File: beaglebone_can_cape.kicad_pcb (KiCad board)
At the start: 2 copper layers, 86.4 x 54.6 mm, 24 parts, among them J1 DCAN0, J2 DCAN1, P8 BeagleBone_Black_Header, P9 BeagleBone_Black_Header, U1 TCAN332, U2 TCAN332, U3 LMR51430

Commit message: PCB and SCH updates
Just moved some text boxes, footprints, and explored ideas for the Deutsch connectors.

Co-Authored-By: Zach Weidner <119375087+weidnerz@users.noreply.github.com>
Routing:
- added copper zone on F.Cu, net +3.3V
- added copper zone on B.Cu, net GNDD
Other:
- board text added: "DCAN0"
- board text added: "DCAN1"
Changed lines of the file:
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@@
 	(net 99 "unconnected-(U2-NC-Pad5)")
 	(footprint "Connector_PinHeader_2.54mm:PinHeader_2x23_P2.54mm_Vertical"
-		(locked yes)
 		(layer "F.Cu")
 		(at 119.685 49.835 90)
@@
 		(tags "Through hole pin header THT 2x23 2.54mm double row")
 		(property "Reference" "P8"
-			(at 1.27 -2.33 270)
+			(at -2.165 0 0)
 			(layer "F.SilkS")
 			(effects
@@
 			)
 			(rotate
-				(xyz 0 0 0)
+				(xyz -0 -0 -0)
 			)
 		)
 	)
 	(footprint "Connector_PinHeader_2.54mm:PinHeader_2x23_P2.54mm_Vertical"
-		(locked yes)
 		(layer "F.Cu")
 		(at 119.685 98.095 90)
@@
 		(tags "Through hole pin header THT 2x23 2.54mm double row")
 		(property "Reference" "P9"
-			(at 1.27 -2.33 270)
+			(at 5.095 0 0)
 			(layer "F.SilkS")
 			(effects
@@
 		)
 	)
+	(gr_text "DCAN1"
+		(at 174.25 86.75 0)
+		(layer "F.SilkS")
+		(effects
+			(font
+				(size 1 1)
+				(thickness 0.15)
+			)
+			(justify left bottom)
+		)
+	)
+	(gr_text "DCAN0"
+		(at 174.25 72.5 0)
+		(layer "F.SilkS")
+		(effects
+			(font
+				(size 1 1)
+				(thickness 0.15)
+			)
+			(justify left bottom)
+		)
+	)
 	(gr_text "CANH"
 		(at 179.5 64 0)
@@
 		(net 89)
 	)
+	(zone
+		(net 89)
+		(net_name "+3.3V")
+		(layer "F.Cu")
+		(hatch edge 0.5)
+		(priority 1)
+		(connect_pads
+			(clearance 0.508)
+		)
+		(min_thickness 0.25)
+		(filled_areas_thickness no)
+		(fill yes
+			(thermal_gap 0.5)
+			(thermal_bridge_width 0.5)
+		)
+		(polygon
+			(pts
+				(xy 97 41) (xy 97 107.25) (xy 188 107.25) (xy 188.75 41.25)
+			)
+		)
+	)
+	(zone
+		(net 50)
+		(net_name "GNDD")
+		(layer "B.Cu")
+		(hatch edge 0.5)
+		(connect_pads
+			(clearance 0.508)
+		)
+		(min_thickness 0.25)
+		(filled_areas_thickness no)
+		(fill yes
+			(thermal_gap 0.5)
+			(thermal_bridge_width 0.5)
+		)
+		(polygon
+			(pts
+				(xy 103 43) (xy 103 53.25) (xy 187.771427 52.999937) (xy 187.5 43.5)
+			)
+		)
+	)
 	(embedded_fonts no)

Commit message: Pushing pcb additions of buckdown, need more work on schem
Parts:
- moved L1 70.9 mm to (136.9, 62.5)
- moved R4 63.0 mm to (133.3, 66.8)
- moved Cout1 56.0 mm to (123.4, 62.5)
- moved R5 54.2 mm to (128.9, 66.8)
- moved U3 52.1 mm to (128.1, 74.4), turned to -90 degrees
- moved Cboot1 50.9 mm to (134.2, 74.3), turned to 90 degrees
- moved Cin1 46.8 mm to (128.1, 70.5)
- moved R3 45.6 mm to (124.7, 66.8)
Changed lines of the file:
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@@
 	(footprint "Inductor_SMD:L_0805_2012Metric"
 		(layer "F.Cu")
-		(at 71.05 88.595)
+		(at 136.9475 62.55)
 		(descr "Inductor SMD 0805 (2012 Metric), square (rectangular) end terminal, IPC-7351 nominal, (Body size source: IPC-SM-782 page 80, https://www.pcb-3d.com/wordpress/wp-content/uploads/ipc-sm-782a_amendment_1_and_2.pdf), generated with kicad-footprint-generator")
 		(tags "inductor")
@@
 	(footprint "Resistor_SMD:R_0805_2012Metric"
 		(layer "F.Cu")
-		(at 71.3375 78.25)
+		(at 133.3125 66.78)
 		(descr "Resistor SMD 0805 (2012 Metric), square (rectangular) end terminal, IPC-7351 nominal, (Body size source: IPC-SM-782 page 72, https://www.pcb-3d.com/wordpress/wp-content/uploads/ipc-sm-782a_amendment_1_and_2.pdf), generated with kicad-footprint-generator")
 		(tags "resistor")
@@
 	(footprint "Capacitor_SMD:C_0805_2012Metric"
 		(layer "F.Cu")
-		(at 71.25 83)
+		(at 123.37 62.55)
 		(descr "Capacitor SMD 0805 (2012 Metric), square (rectangular) end terminal, IPC-7351 nominal, (Body size source: IPC-SM-782 page 76, https://www.pcb-3d.com/wordpress/wp-content/uploads/ipc-sm-782a_amendment_1_and_2.pdf, https://docs.google.com/spreadsheets/d/1BsfQQcO9C6DZCsRaXUlFlo91Tg2WpOkGARC1WS5S8t0/edit?usp=sharing), generated with kicad-footprint-generator")
 		(tags "capacitor")
@@
 	(footprint "Package_TO_SOT_SMD:SOT-23-6"
 		(layer "F.Cu")
-		(at 77.3625 86.05)
+		(at 128.14 74.41 -90)
 		(descr "SOT, 6 Pin (JEDEC MO-178 Var AB https://www.jedec.org/document_search?search_api_views_fulltext=MO-178), generated with kicad-footprint-generator ipc_gullwing_generator.py")
 		(tags "SOT TO_SOT_SMD")
 		(property "Reference" "U3"
-			(at 0 -2.4 0)
+			(at 0 -2.4 90)
 			(layer "F.SilkS")
 			(effects
@@
 		)
 		(property "Value" "LMR51430"
-			(at 0 2.4 0)
+			(at 0 2.4 90)
 			(layer "F.Fab")
 			(effects
@@
 		)
 		(property "Datasheet" "https://www.ti.com/lit/ds/symlink/lmr51430.pdf"
-			(at 0 0 0)
+			(at 0 0 90)
 			(layer "F.Fab")
 			(hide yes)
@@
 		)
 		(property "Description" "4.5-V to 36-V, 3-A synchronous buck converter with 40-µA IQ, SOT-23-6"
-			(at 0 0 0)
+			(at 0 0 90)
 			(layer "F.Fab")
 			(hide yes)
@@
 		(attr smd)
 		(fp_line
-			(start 0 -1.56)
-			(end -0.8 -1.56)
+			(start 0 1.56)
+			(end -0.8 1.56)
 			(stroke
 				(width 0.12)
@@
 		)
 		(fp_line
-			(start 0 -1.56)
-			(end 0.8 -1.56)
+			(start 0 1.56)
+			(end 0.8 1.56)
 			(stroke
 				(width 0.12)
@@
 		)
 		(fp_line
-			(start 0 1.56)
-			(end -0.8 1.56)
+			(start 0 -1.56)
+			(end -0.8 -1.56)
 			(stroke
 				(width 0.12)
@@
 		)
 		(fp_line
-			(start 0 1.56)
-			(end 0.8 1.56)
+			(start 0 -1.56)
+			(end 0.8 -1.56)
 			(stroke
 				(width 0.12)
@@
 		)
 		(fp_line
-			(start -2.05 -1.5)
-			(end -1.05 -1.5)
+			(start -1.05 1.7)
+			(end -1.05 1.5)
 			(stroke
 				(width 0.05)
@@
 		)
 		(fp_line
-			(start -2.05 1.5)
-			(end -2.05 -1.5)
+			(start 1.05 1.7)
+			(end -1.05 1.7)
 			(stroke
 				(width 0.05)
@@
 		)
 		(fp_line
-			(start -1.05 -1.7)
-			(end 1.05 -1.7)
+			(start -2.05 1.5)
+			(end -2.05 -1.5)
 			(stroke
 				(width 0.05)
@@
 		)
 		(fp_line
-			(start -1.05 -1.5)
-			(end -1.05 -1.7)
+			(start -1.05 1.5)
+			(end -2.05 1.5)
 			(stroke
 				(width 0.05)
@@
 		)
 		(fp_line
-			(start -1.05 1.5)
-			(end -2.05 1.5)
+			(start 1.05 1.5)
+			(end 1.05 1.7)
 			(stroke
 				(width 0.05)
@@
 		)
 		(fp_line
-			(start -1.05 1.7)
-			(end -1.05 1.5)
+			(start 2.05 1.5)
+			(end 1.05 1.5)
 			(stroke
 				(width 0.05)
@@
 		)
 		(fp_line
-			(start 1.05 -1.7)
-			(end 1.05 -1.5)
+			(start -2.05 -1.5)
+			(end -1.05 -1.5)
 			(stroke
 				(width 0.05)
@@
 		)
 		(fp_line
-			(start 1.05 -1.5)
-			(end 2.05 -1.5)
+			(start -1.05 -1.5)
+			(end -1.05 -1.7)
 			(stroke
 				(width 0.05)
@@
 		)
 		(fp_line
-			(start 1.05 1.5)
-			(end 1.05 1.7)
+			(start 1.05 -1.5)
+			(end 2.05 -1.5)
 			(stroke
 				(width 0.05)
@@
 		)
 		(fp_line
-			(start 1.05 1.7)
-			(end -1.05 1.7)
+			(start 2.05 -1.5)
+			(end 2.05 1.5)
 			(stroke
 				(width 0.05)
@@
 		)
 		(fp_line
-			(start 2.05 -1.5)
-			(end 2.05 1.5)
+			(start -1.05 -1.7)
+			(end 1.05 -1.7)
 			(stroke
 				(width 0.05)
@@
 		)
 		(fp_line
-			(start 2.05 1.5)
-			(end 1.05 1.5)
+			(start 1.05 -1.7)
+			(end 1.05 -1.5)
 			(stroke
 				(width 0.05)
@@
 		)
 		(fp_text user "${REFERENCE}"
-			(at 0 0 0)
+			(at 0 0 90)
 			(layer "F.Fab")
 			(effects
@@
 		)
 		(pad "1" smd roundrect
-			(at -1.1375 -0.95)
+			(at -1.1375 -0.95 270)
 			(size 1.325 0.6)
 			(layers "F.Cu" "F.Mask" "F.Paste")
@@
 		)
 		(pad "2" smd roundrect
-			(at -1.1375 0)
+			(at -1.1375 0 270)
 			(size 1.325 0.6)
 			(layers "F.Cu" "F.Mask" "F.Paste")
@@
 		)
 		(pad "3" smd roundrect
-			(at -1.1375 0.95)
+			(at -1.1375 0.95 270)
 			(size 1.325 0.6)
 			(layers "F.Cu" "F.Mask" "F.Paste")
@@
 		)
 		(pad "4" smd roundrect
-			(at 1.1375 0.95)
+			(at 1.1375 0.95 270)
 			(size 1.325 0.6)
 			(layers "F.Cu" "F.Mask" "F.Paste")
@@
 		)
 		(pad "5" smd roundrect
-			(at 1.1375 0)
+			(at 1.1375 0 270)
 			(size 1.325 0.6)
 			(layers "F.Cu" "F.Mask" "F.Paste")
@@
 		)
 		(pad "6" smd roundrect
-			(at 1.1375 -0.95)
+			(at 1.1375 -0.95 270)
 			(size 1.325 0.6)
 			(layers "F.Cu" "F.Mask" "F.Paste")
@@
 	(footprint "Capacitor_SMD:C_0805_2012Metric"
 		(layer "F.Cu")
-		(at 84.25 86.76)
+		(at 128.14 70.47)
 		(descr "Capacitor SMD 0805 (2012 Metric), square (rectangular) end terminal, IPC-7351 nominal, (Body size source: IPC-SM-782 page 76, https://www.pcb-3d.com/wordpress/wp-content/uploads/ipc-sm-782a_amendment_1_and_2.pdf, https://docs.google.com/spreadsheets/d/1BsfQQcO9C6DZCsRaXUlFlo91Tg2WpOkGARC1WS5S8t0/edit?usp=sharing), generated with kicad-footprint-generator")
 		(tags "capacitor")
@@
 	(footprint "Capacitor_SMD:C_0805_2012Metric"
 		(layer "F.Cu")
-		(at 84.25 83.75)
+		(at 134.23 74.34 90)
 		(descr "Capacitor SMD 0805 (2012 Metric), square (rectangular) end terminal, IPC-7351 nominal, (Body size source: IPC-SM-782 page 76, https://www.pcb-3d.com/wordpress/wp-content/uploads/ipc-sm-782a_amendment_1_and_2.pdf, https://docs.google.com/spreadsheets/d/1BsfQQcO9C6DZCsRaXUlFlo91Tg2WpOkGARC1WS5S8t0/edit?usp=sharing), generated with kicad-footprint-generator")
 		(tags "capacitor")
 		(property "Reference" "Cboot1"
-			(at 0 -1.68 0)
+			(at 0 -1.68 90)
 			(layer "F.SilkS")
 			(effects
@@
 		)
 		(property "Value" "0.1 uF"
-			(at 0 1.68 0)
+			(at 0 1.68 90)
 			(layer "F.Fab")
 			(effects
@@
 		)
 		(property "Datasheet" "~"
-			(at 0 0 0)
+			(at 0 0 90)
 			(layer "F.Fab")
 			(hide yes)
@@
 		)
 		(property "Description" "Unpolarized capacitor, small symbol"
-			(at 0 0 0)
+			(at 0 0 90)
 			(layer "F.Fab")
 			(hide yes)
@@
 		)
 		(fp_line
-			(start -1.7 -0.98)
-			(end 1.7 -0.98)
+			(start 1.7 -0.98)
+			(end 1.7 0.98)
 			(stroke
 				(width 0.05)
@@
 		)
 		(fp_line
-			(start -1.7 0.98)
-			(end -1.7 -0.98)
+			(start -1.7 -0.98)
+			(end 1.7 -0.98)
 			(stroke
 				(width 0.05)
@@
 		)
 		(fp_line
-			(start 1.7 -0.98)
-			(end 1.7 0.98)
+			(start 1.7 0.98)
+			(end -1.7 0.98)
 			(stroke
 				(width 0.05)
@@
 		)
 		(fp_line
-			(start 1.7 0.98)
-			(end -1.7 0.98)
+			(start -1.7 0.98)
+			(end -1.7 -0.98)
 			(stroke
 				(width 0.05)
@@
 		)
 		(fp_line
-			(start -1 -0.625)
-			(end 1 -0.625)
+			(start 1 -0.625)
+			(end 1 0.625)
 			(stroke
 				(width 0.1)
@@
 		)
 		(fp_line
-			(start -1 0.625)
-			(end -1 -0.625)
+			(start -1 -0.625)
+			(end 1 -0.625)
 			(stroke
 				(width 0.1)
@@
 		)
 		(fp_line
-			(start 1 -0.625)
-			(end 1 0.625)
+			(start 1 0.625)
+			(end -1 0.625)
 			(stroke
 				(width 0.1)
@@
 		)
 		(fp_line
-			(start 1 0.625)
-			(end -1 0.625)
+			(start -1 0.625)
+			(end -1 -0.625)
 			(stroke
 				(width 0.1)
@@
 		)
 		(fp_text user "${REFERENCE}"
-			(at 0 0 0)
+			(at 0 0 90)
 			(layer "F.Fab")
 			(effects
@@
 		)
 		(pad "1" smd roundrect
-			(at -0.95 0)
+			(at -0.95 0 90)
 			(size 1 1.45)
 			(layers "F.Cu" "F.Mask" "F.Paste")
@@
 		)
 		(pad "2" smd roundrect
-			(at 0.95 0)
+			(at 0.95 0 90)
 			(size 1 1.45)
 			(layers "F.Cu" "F.Mask" "F.Paste")
@@
 	(footprint "Resistor_SMD:R_0805_2012Metric"
 		(layer "F.Cu")
-		(at 80.3375 77.5)
+		(at 124.67 66.77)
 		(descr "Resistor SMD 0805 (2012 Metric), square (rectangular) end terminal, IPC-7351 nominal, (Body size source: IPC-SM-782 page 72, https://www.pcb-3d.com/wordpress/wp-content/uploads/ipc-sm-782a_amendment_1_and_2.pdf), generated with kicad-footprint-generator")
 		(tags "resistor")
@@
 	(footprint "Resistor_SMD:R_0805_2012Metric"
 		(layer "F.Cu")
-		(at 76.3375 80)
+		(at 128.94 66.77)
 		(descr "Resistor SMD 0805 (2012 Metric), square (rectangular) end terminal, IPC-7351 nominal, (Body size source: IPC-SM-782 page 72, https://www.pcb-3d.com/wordpress/wp-content/uploads/ipc-sm-782a_amendment_1_and_2.pdf), generated with kicad-footprint-generator")
 		(tags "resistor")
 		(property "Reference" "R5"
-			(at 0 -1.65 0)
+			(at 0.1125 -2.5 0)
 			(layer "F.SilkS")
 			(effects

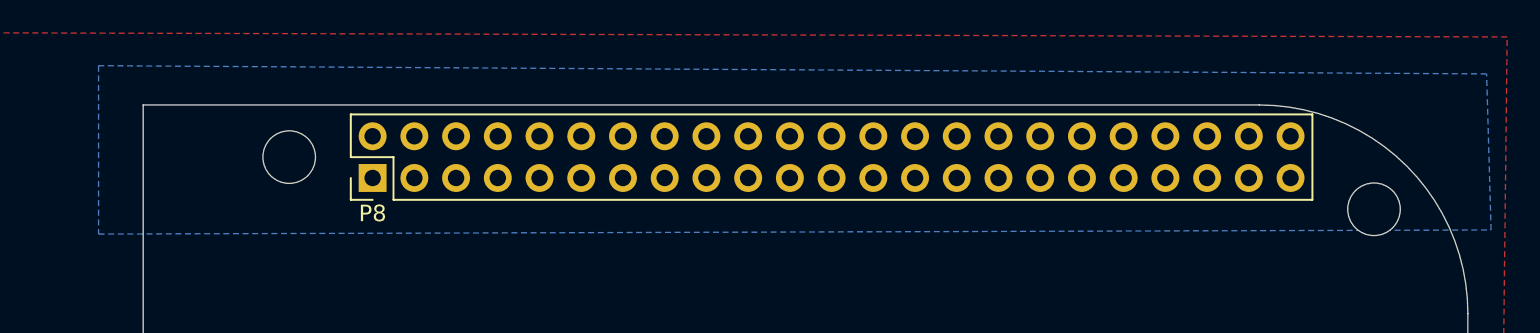
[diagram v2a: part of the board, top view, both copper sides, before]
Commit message: Removed temp gnd plane b.cu
nuff said
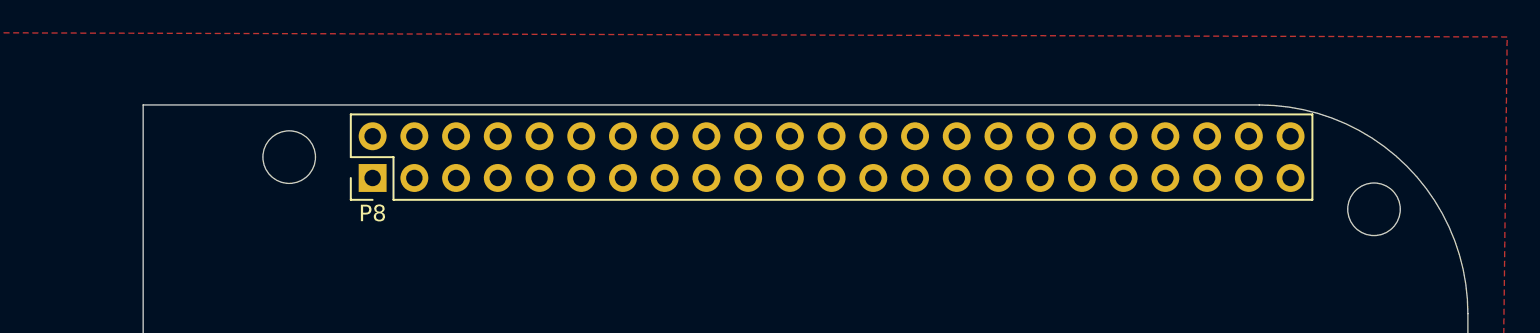
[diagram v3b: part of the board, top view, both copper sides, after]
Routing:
- removed copper zone on B.Cu, net GNDD
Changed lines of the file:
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@@
-		)
-	)
-	(zone
-		(net 50)
-		(net_name "GNDD")
-		(layer "B.Cu")
-		(hatch edge 0.5)
-		(connect_pads
-			(clearance 0.508)
-		)
-		(min_thickness 0.25)
-		(filled_areas_thickness no)
-		(fill yes
-			(thermal_gap 0.5)
-			(thermal_bridge_width 0.5)
-		)
-		(polygon
-			(pts
-				(xy 103 43) (xy 103 53.25) (xy 187.771427 52.999937) (xy 187.5 43.5)
-			)
 		)
 	)
